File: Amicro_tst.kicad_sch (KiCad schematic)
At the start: 38 parts, among them J1 Sensor, J2 Progm, J3 Vibr, J4 Pow, Q1 Q_NPN_BEC, Q2 Q_NPN_BEC, Q3 Q_NPN_BEC, Q4 Q_NPN_BEC, SW1 RESET, U1 ATmega328-P, U2 24LC512, Y1 Crystal

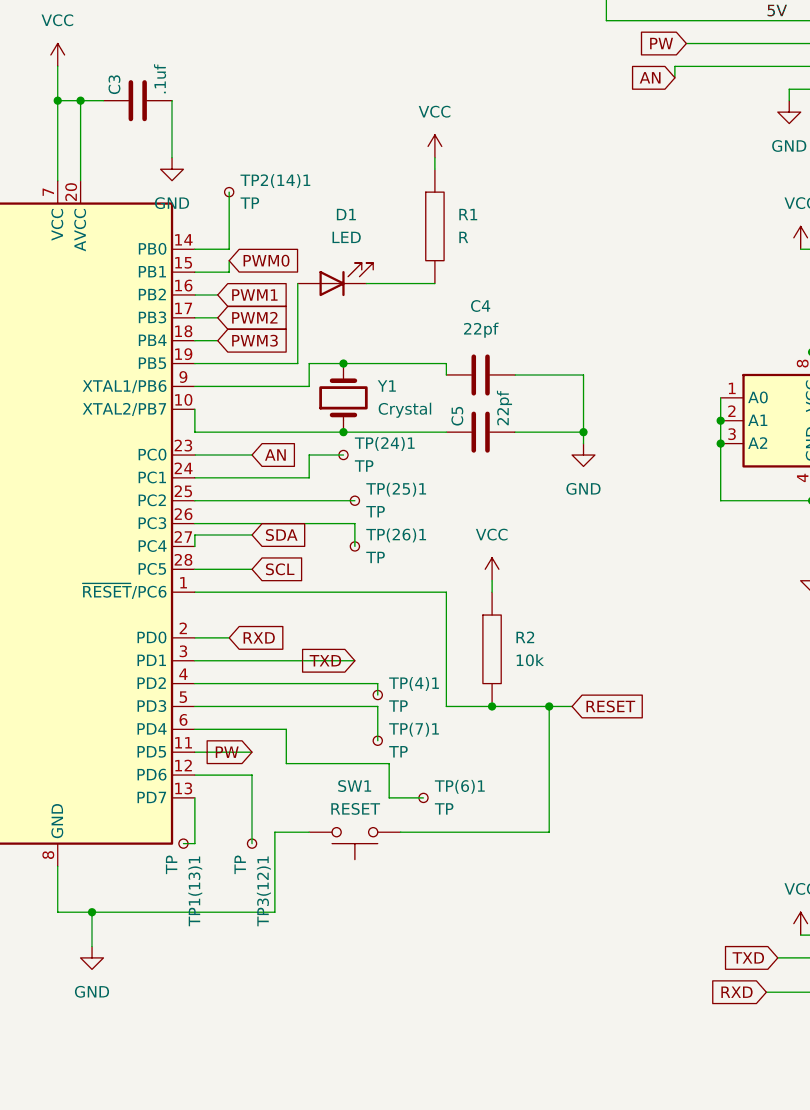
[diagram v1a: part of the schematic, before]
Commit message: Hole Alignment And Added tstpnt
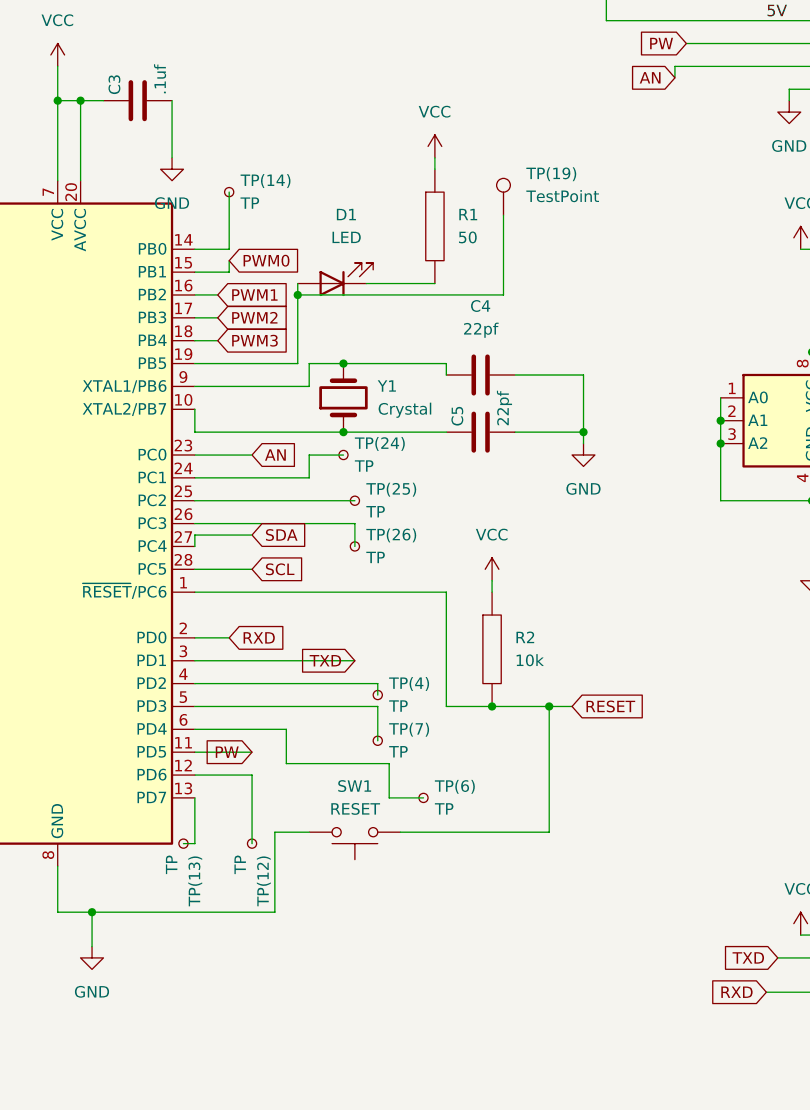
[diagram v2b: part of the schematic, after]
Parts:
- added TP(19): TestPoint, symbol Connector:TestPoint
- R1: value R -> 50
- renumbered TP3(12)1 to TP(12), TP1(13)1 to TP(13), TP2(14)1 to TP(14), TP(24)1 to TP(24), TP(25)1 to TP(25), TP(26)1 to TP(26), TP(4)1 to TP(4), TP(6)1 to TP(6), TP(7)1 to TP(7)
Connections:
- net at D1.2 (A), U1.19 (PB5): now also TP(19).1
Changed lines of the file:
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@@
   (junction (at 139.7 101.6) (diameter 0) (color 0 0 0 0)
   )
+  (junction (at 92.71 87.63) (diameter 0) (color 0 0 0 0)
+  )
   (junction (at 66.04 66.04) (diameter 0) (color 0 0 0 0)
   )
@@
     (stroke (width 0) (type default) (color 0 0 0 0))
   )
+  (wire (pts (xy 115.57 87.63) (xy 92.71 87.63))
+    (stroke (width 0) (type default) (color 0 0 0 0))
+  )
   (wire (pts (xy 194.31 100.33) (xy 196.85 100.33))
     (stroke (width 0) (type default) (color 0 0 0 0))
@@
     (stroke (width 0) (type default) (color 0 0 0 0))
   )
-  (wire (pts (xy 92.71 86.36) (xy 92.71 95.25))
+  (wire (pts (xy 92.71 86.36) (xy 92.71 87.63))
     (stroke (width 0) (type default) (color 0 0 0 0))
   )
@@
     (stroke (width 0) (type default) (color 0 0 0 0))
   )
+  (wire (pts (xy 92.71 87.63) (xy 92.71 95.25))
+    (stroke (width 0) (type default) (color 0 0 0 0))
+  )
   (wire (pts (xy 107.95 72.39) (xy 107.95 73.66))
     (stroke (width 0) (type default) (color 0 0 0 0))
@@
   )
   (wire (pts (xy 190.5 119.38) (xy 194.31 119.38))
+    (stroke (width 0) (type default) (color 0 0 0 0))
+  )
+  (wire (pts (xy 115.57 78.74) (xy 115.57 87.63))
     (stroke (width 0) (type default) (color 0 0 0 0))
   )
@@
   (symbol (lib_id "Connector:TestPoint_Small") (at 80.01 148.59 270) (unit 1)
     (in_bom yes) (on_board yes)
-    (property "Reference" "TP1(13)1" (id 0) (at 81.2801 149.86 0)
+    (property "Reference" "TP(13)" (id 0) (at 81.2801 149.86 0)
       (effects (font (size 1.27 1.27)) (justify left))
     )
@@
   (symbol (lib_id "Connector:TestPoint_Small") (at 85.09 76.2 0) (unit 1)
     (in_bom yes) (on_board yes)
-    (property "Reference" "TP2(14)1" (id 0) (at 86.36 74.9299 0)
+    (property "Reference" "TP(14)" (id 0) (at 86.36 74.9299 0)
       (effects (font (size 1.27 1.27)) (justify left))
     )
@@
   )
   (symbol (lib_id "pspice:R") (at 107.95 80.01 0) (unit 1)
-    (in_bom yes) (on_board yes) (fields_autoplaced)
+    (in_bom yes) (on_board yes)
     (property "Reference" "R1" (id 0) (at 110.49 78.7399 0)
       (effects (font (size 1.27 1.27)) (justify left))
     )
-    (property "Value" "R" (id 1) (at 110.49 81.2799 0)
+    (property "Value" "50" (id 1) (at 110.49 81.2799 0)
       (effects (font (size 1.27 1.27)) (justify left))
     )
@@
   (symbol (lib_id "Connector:TestPoint_Small") (at 87.63 148.59 270) (unit 1)
     (in_bom yes) (on_board yes)
-    (property "Reference" "TP3(12)1" (id 0) (at 88.9001 149.86 0)
+    (property "Reference" "TP(12)" (id 0) (at 88.9001 149.86 0)
       (effects (font (size 1.27 1.27)) (justify left))
     )
@@
   (symbol (lib_id "Connector:TestPoint_Small") (at 99.06 110.49 0) (unit 1)
     (in_bom yes) (on_board yes)
-    (property "Reference" "TP(25)1" (id 0) (at 100.33 109.2199 0)
+    (property "Reference" "TP(25)" (id 0) (at 100.33 109.2199 0)
       (effects (font (size 1.27 1.27)) (justify left))
     )
@@
   (symbol (lib_id "Connector:TestPoint_Small") (at 106.68 143.51 0) (unit 1)
     (in_bom yes) (on_board yes)
-    (property "Reference" "TP(6)1" (id 0) (at 107.95 142.2399 0)
+    (property "Reference" "TP(6)" (id 0) (at 107.95 142.2399 0)
       (effects (font (size 1.27 1.27)) (justify left))
     )
@@
   (symbol (lib_id "Connector:TestPoint_Small") (at 101.6 132.08 0) (unit 1)
     (in_bom yes) (on_board yes)
-    (property "Reference" "TP(4)1" (id 0) (at 102.87 130.8099 0)
+    (property "Reference" "TP(4)" (id 0) (at 102.87 130.8099 0)
       (effects (font (size 1.27 1.27)) (justify left))
     )
@@
     (pin "1")
     (pin "2")
+  )
+  (symbol (lib_id "Connector:TestPoint") (at 115.57 78.74 0) (unit 1)
+    (in_bom yes) (on_board yes) (fields_autoplaced)
+    (property "Reference" "TP(19)" (id 0) (at 118.11 74.1679 0)
+      (effects (font (size 1.27 1.27)) (justify left))
+    )
+    (property "Value" "TestPoint" (id 1) (at 118.11 76.7079 0)
+      (effects (font (size 1.27 1.27)) (justify left))
+    )
+    (property "Footprint" "" (id 2) (at 120.65 78.74 0)
+      (effects (font (size 1.27 1.27)) hide)
+    )
+    (property "Datasheet" "~" (id 3) (at 120.65 78.74 0)
+      (effects (font (size 1.27 1.27)) hide)
+    )
+    (pin "1")
   )
   (symbol (lib_id "power:VCC") (at 280.67 139.7 0) (unit 1)
@@
   (symbol (lib_id "Connector:TestPoint_Small") (at 97.79 105.41 0) (unit 1)
     (in_bom yes) (on_board yes)
-    (property "Reference" "TP(24)1" (id 0) (at 99.06 104.1399 0)
+    (property "Reference" "TP(24)" (id 0) (at 99.06 104.1399 0)
       (effects (font (size 1.27 1.27)) (justify left))
     )
@@
   (symbol (lib_id "Connector:TestPoint_Small") (at 99.06 115.57 0) (unit 1)
     (in_bom yes) (on_board yes)
-    (property "Reference" "TP(26)1" (id 0) (at 100.33 114.2999 0)
+    (property "Reference" "TP(26)" (id 0) (at 100.33 114.2999 0)
       (effects (font (size 1.27 1.27)) (justify left))
     )
@@
   (symbol (lib_id "Connector:TestPoint_Small") (at 101.6 137.16 0) (unit 1)
     (in_bom yes) (on_board yes)
-    (property "Reference" "TP(7)1" (id 0) (at 102.87 135.8899 0)
+    (property "Reference" "TP(7)" (id 0) (at 102.87 135.8899 0)
       (effects (font (size 1.27 1.27)) (justify left))
     )
@@
     )
     (path "/2719589e-6f3e-41f2-ae58-0c107b009320"
-      (reference "R1") (unit 1) (value "R") (footprint "Resistor_SMD:R_0402_1005Metric")
+      (reference "R1") (unit 1) (value "50") (footprint "Resistor_SMD:R_0402_1005Metric")
     )
     (path "/bc02e175-2ba0-4b50-83cf-01e6a8d434ed"
@@
     )
     (path "/57803f16-4951-4322-937a-3335afb08842"
-      (reference "TP(4)1") (unit 1) (value "TP") (footprint "TestPoint:TestPoint_THTPad_1.0x1.0mm_Drill0.5mm")
+      (reference "TP(4)") (unit 1) (value "TP") (footprint "TestPoint:TestPoint_THTPad_1.0x1.0mm_Drill0.5mm")
     )
     (path "/463e4c84-30ed-487f-958a-8d35a40efe38"
-      (reference "TP(6)1") (unit 1) (value "TP") (footprint "TestPoint:TestPoint_THTPad_1.0x1.0mm_Drill0.5mm")
+      (reference "TP(6)") (unit 1) (value "TP") (footprint "TestPoint:TestPoint_THTPad_1.0x1.0mm_Drill0.5mm")
     )
     (path "/d747968d-1725-40a5-bf12-3208d9131768"
-      (reference "TP(7)1") (unit 1) (value "TP") (footprint "TestPoint:TestPoint_THTPad_1.0x1.0mm_Drill0.5mm")
+      (reference "TP(7)") (unit 1) (value "TP") (footprint "TestPoint:TestPoint_THTPad_1.0x1.0mm_Drill0.5mm")
+    )
+    (path "/3afe24a8-dc8f-418b-8ea7-f4d6e4f519c6"
+      (reference "TP(12)") (unit 1) (value "TP") (footprint "TestPoint:TestPoint_THTPad_1.0x1.0mm_Drill0.5mm")
+    )
+    (path "/05ab7aa5-7b8e-4104-a8d0-893eabc178ac"
+      (reference "TP(13)") (unit 1) (value "TP") (footprint "TestPoint:TestPoint_THTPad_1.0x1.0mm_Drill0.5mm")
+    )
+    (path "/1e8636dc-257b-4ddd-a4ee-08d597e947fe"
+      (reference "TP(14)") (unit 1) (value "TP") (footprint "TestPoint:TestPoint_THTPad_1.0x1.0mm_Drill0.5mm")
+    )
+    (path "/654beb0c-1bb6-4ccb-9b7c-c689f185edc1"
+      (reference "TP(19)") (unit 1) (value "TestPoint") (footprint "")
     )
     (path "/8ca58ff6-3d0e-4962-8f97-a2d132bb9ca5"
-      (reference "TP(24)1") (unit 1) (value "TP") (footprint "TestPoint:TestPoint_THTPad_1.0x1.0mm_Drill0.5mm")
+      (reference "TP(24)") (unit 1) (value "TP") (footprint "TestPoint:TestPoint_THTPad_1.0x1.0mm_Drill0.5mm")
     )
     (path "/3be7a91a-0e4e-4700-b7a6-05629a300185"
-      (reference "TP(25)1") (unit 1) (value "TP") (footprint "TestPoint:TestPoint_THTPad_1.0x1.0mm_Drill0.5mm")
+      (reference "TP(25)") (unit 1) (value "TP") (footprint "TestPoint:TestPoint_THTPad_1.0x1.0mm_Drill0.5mm")
     )
     (path "/bfc17877-a75d-4438-bd98-4babebb460e0"
-      (reference "TP(26)1") (unit 1) (value "TP") (footprint "TestPoint:TestPoint_THTPad_1.0x1.0mm_Drill0.5mm")
-    )
-    (path "/05ab7aa5-7b8e-4104-a8d0-893eabc178ac"
-      (reference "TP1(13)1") (unit 1) (value "TP") (footprint "TestPoint:TestPoint_THTPad_1.0x1.0mm_Drill0.5mm")
-    )
-    (path "/1e8636dc-257b-4ddd-a4ee-08d597e947fe"
-      (reference "TP2(14)1") (unit 1) (value "TP") (footprint "TestPoint:TestPoint_THTPad_1.0x1.0mm_Drill0.5mm")
-    )
-    (path "/3afe24a8-dc8f-418b-8ea7-f4d6e4f519c6"
-      (reference "TP3(12)1") (unit 1) (value "TP") (footprint "TestPoint:TestPoint_THTPad_1.0x1.0mm_Drill0.5mm")
+      (reference "TP(26)") (unit 1) (value "TP") (footprint "TestPoint:TestPoint_THTPad_1.0x1.0mm_Drill0.5mm")
     )
     (path "/6edf16be-7bba-4219-b66e-987d0571c267"

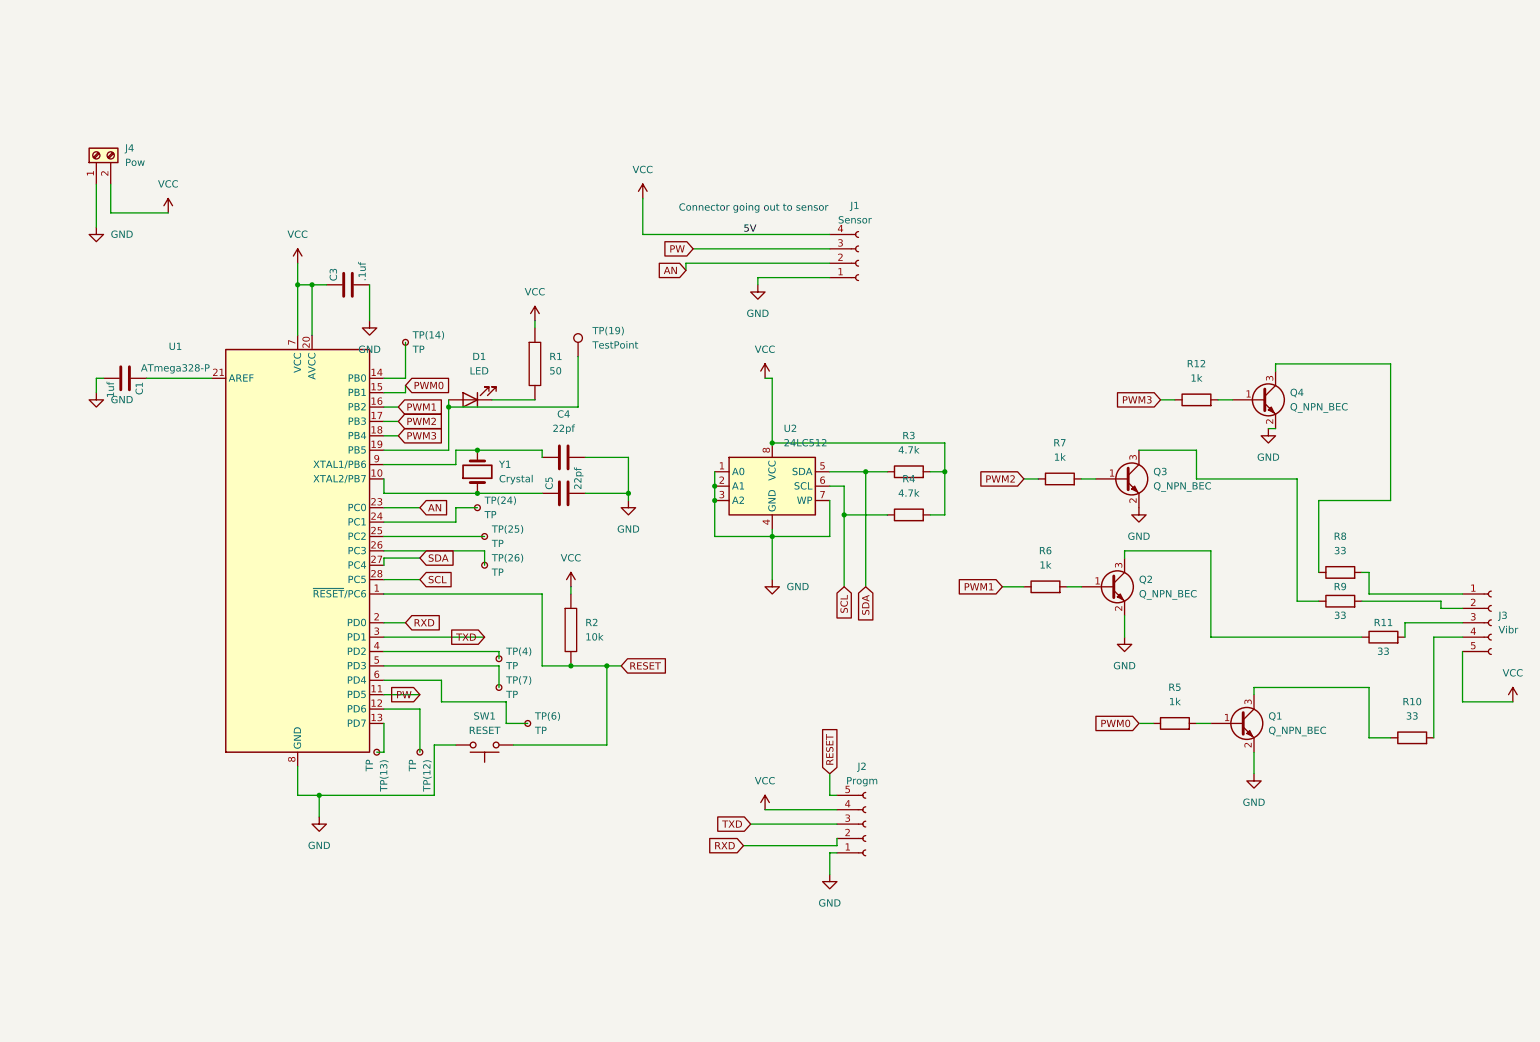
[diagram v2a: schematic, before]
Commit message: Motor schem Wrong, need redo
old gerber files available, messed up on motor schematic, fixed schematic, need to rewire and fix board
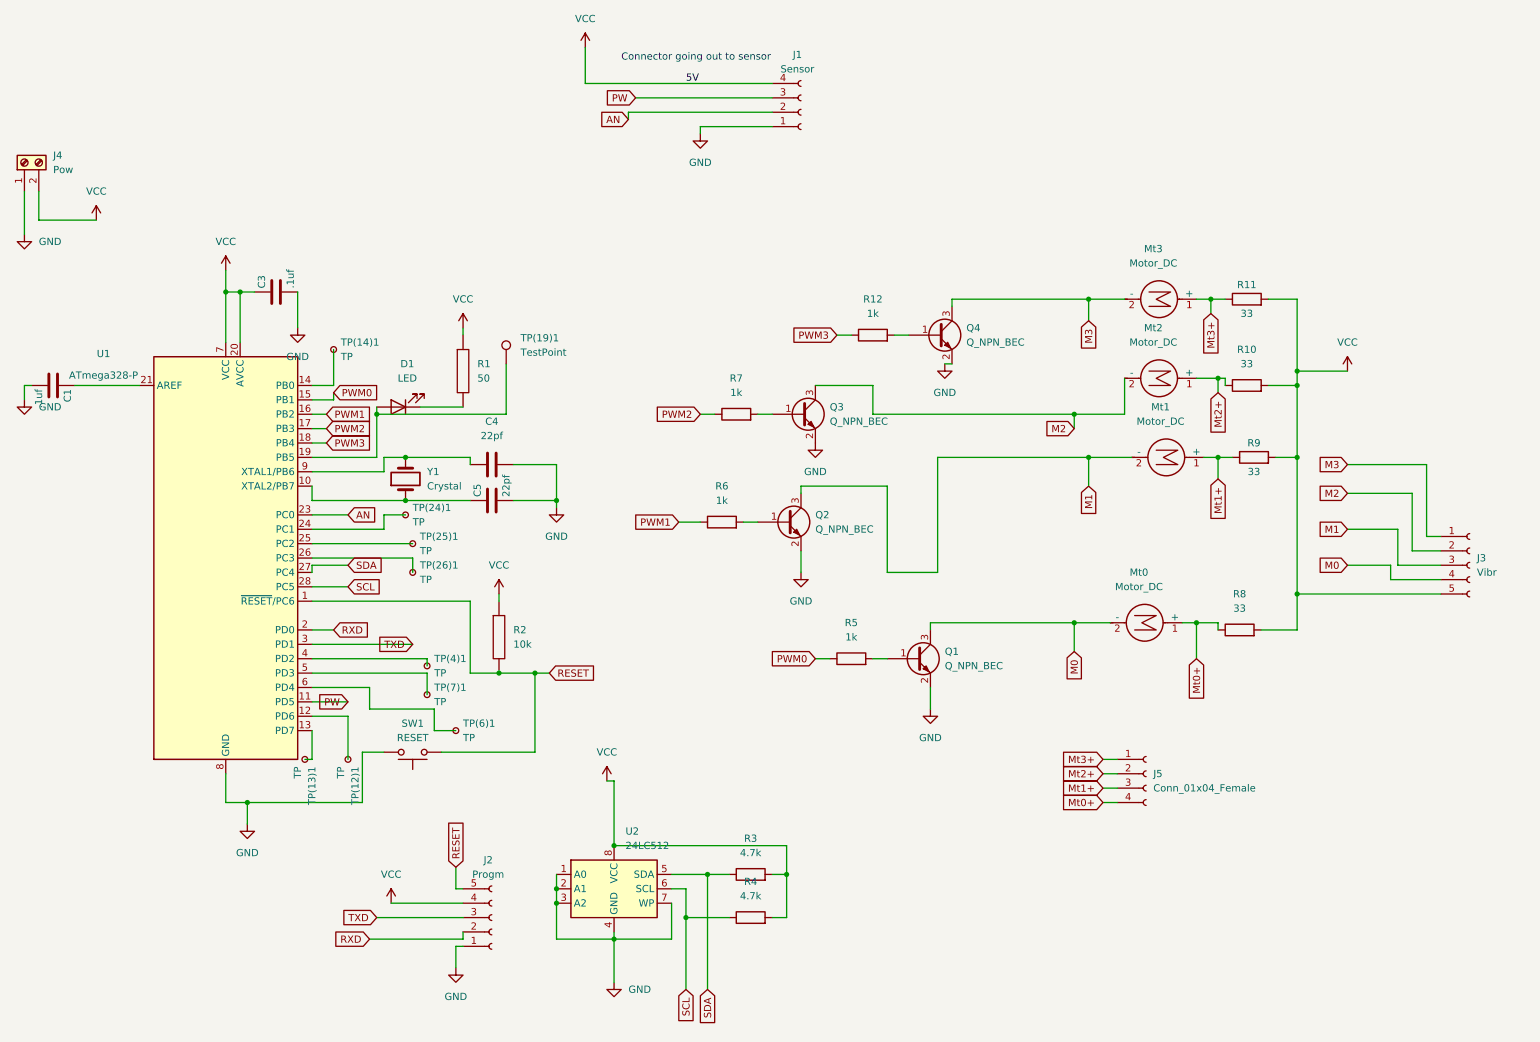
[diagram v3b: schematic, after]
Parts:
- added J5: Conn_01x04_Female, Connector_PinSocket_1.00mm:PinSocket_1x04_P1.00mm_Vertical, symbol Connector:Conn_01x04_Female
- added Mt0, Mt1, Mt2, Mt3: Motor_DC, symbol Motor:Motor_DC
- renumbered TP(12) to TP(12)1, TP(13) to TP(13)1, TP(14) to TP(14)1, TP(19) to TP(19)1, TP(24) to TP(24)1, TP(25) to TP(25)1, TP(26) to TP(26)1, TP(4) to TP(4)1, TP(6) to TP(6)1, TP(7) to TP(7)1
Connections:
- net VCC: now also R10.2, R11.2, R8.2, R9.2
- net M3: now reaches Q4.3 (C)
- net M3: now also J3.1 (Pin_1), Mt3.2 (-); no longer R8.1
- net M1: now reaches Q2.3 (C)
- net M1: now also J3.3 (Pin_3), Mt1.2 (-); no longer R11.1
- net M2: now reaches Q3.3 (C)
- net M2: now also J3.2 (Pin_2), Mt2.2 (-); no longer R9.1
- net M0: now reaches Q1.3 (C)
- net M0: now also J3.4 (Pin_4), Mt0.2 (-); no longer R10.1
- new net Mt0+: J5.4 (Pin_4), Mt0.1 (+), R8.1
- new net Mt1+: J5.3 (Pin_3), Mt1.1 (+), R9.1
- new net Mt2+: J5.2 (Pin_2), Mt2.1 (+), R10.1
- new net Mt3+: J5.1 (Pin_1), Mt3.1 (+), R11.1
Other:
- moved on the sheet: C1, C3, C4, C5, D1, J1, J2, J3, J4, Q1, Q2, Q3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
